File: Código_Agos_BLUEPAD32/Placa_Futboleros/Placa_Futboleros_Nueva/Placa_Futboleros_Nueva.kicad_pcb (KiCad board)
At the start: 2 copper layers, 72 x 72 mm, 18 parts, among them J1 BAT, J2 Motor_Izq_Adelante, J3 Motor_Izq_Atras, J4 Motor_Der_Adelante, J5 Motor_Der_Atras, U1 AMS1117, U2 esp32_36_pins-custom_library, U3 DRV8833, U4 DRV8833

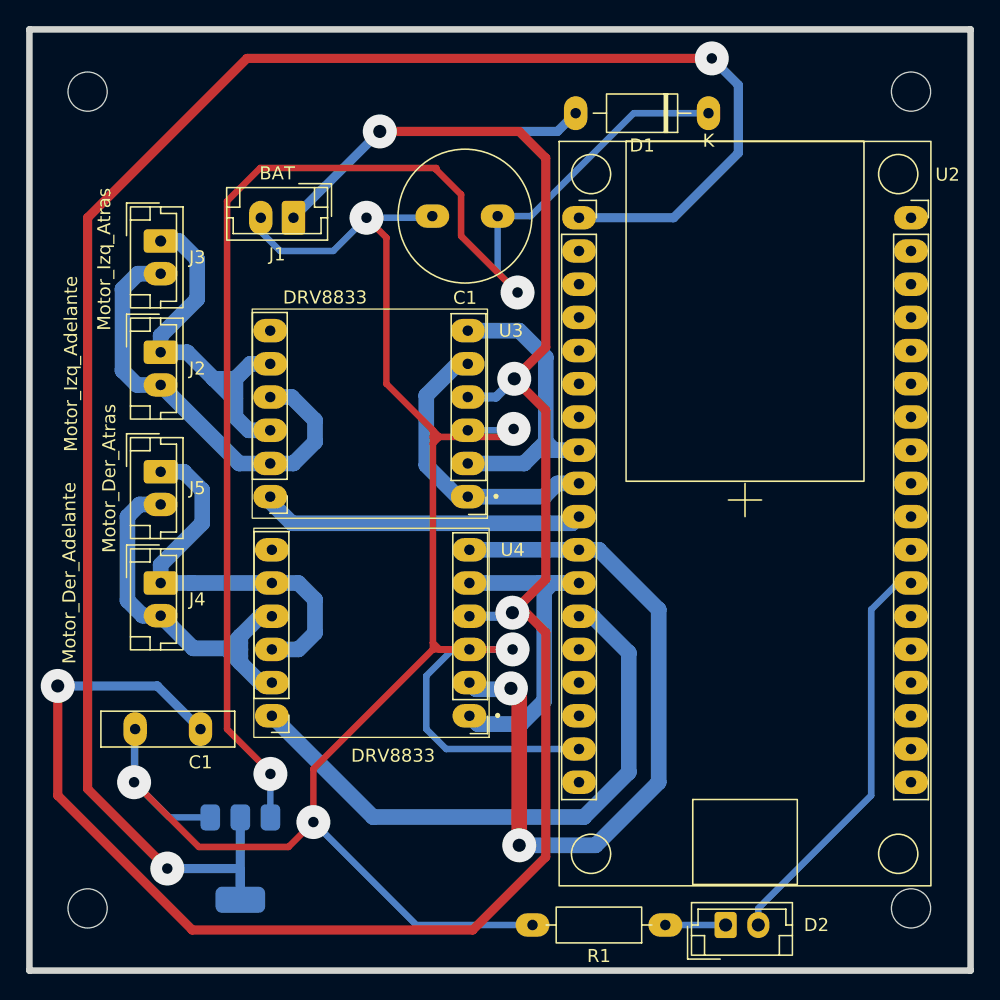
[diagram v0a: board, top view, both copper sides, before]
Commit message: Reorganización de carpetas
Se reordena algunas carpetas para mayor entendimiento...

También se adiciona el archivo original con links importantes
que contienen la información desde donde se empezó este proyecto.
> Tener en cuenta que algunos links pueden ya no estar disponibles, revisar.
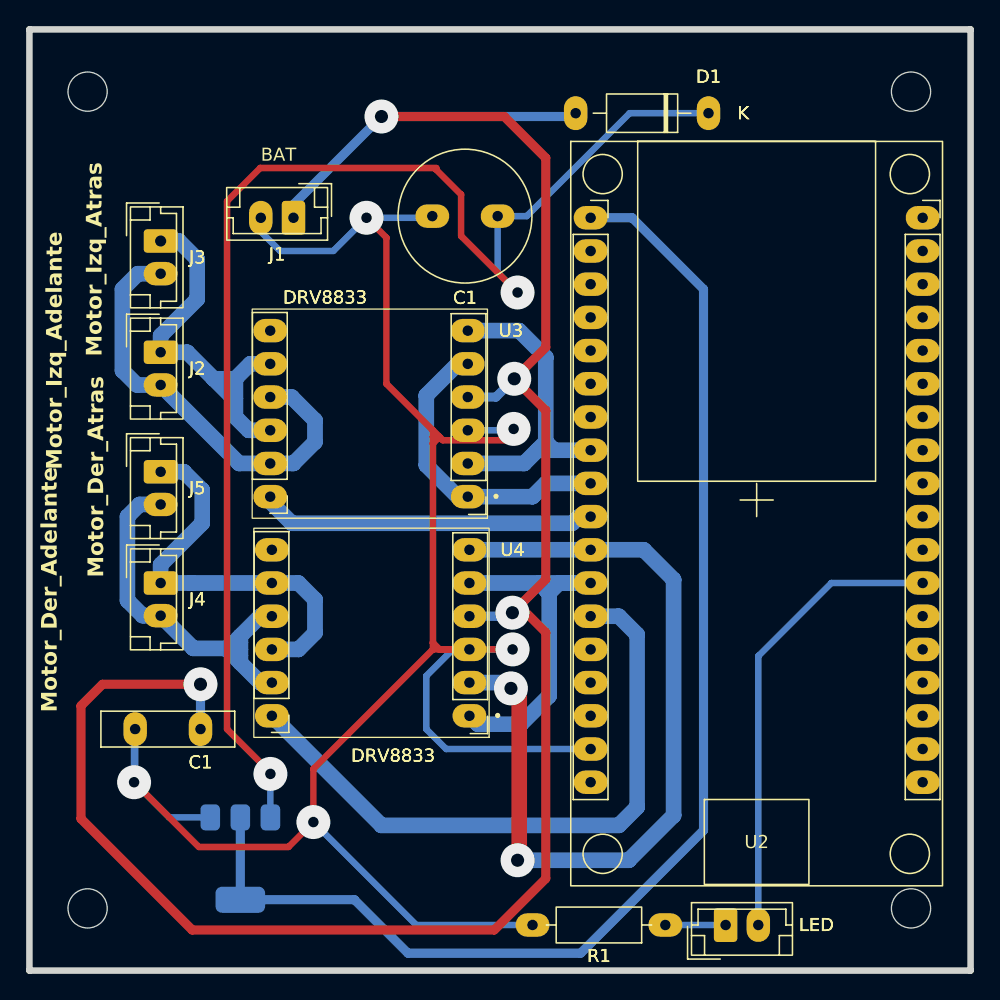
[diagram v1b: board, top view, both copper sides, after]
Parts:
- moved U2 0.89 mm to (109.1, 46.7)
- renumbered D2 to LED
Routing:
- net +5V: track 141.7 -> 99.6 mm, vias 2 -> 0
- net IN_M2B: track 57.9 -> 64.8 mm
- net LED_Encendido: track 31.6 -> 35.5 mm
- net SLEEP_M2: track 46.0 -> 49.3 mm
- net IN_M2A: track 27.1 -> 29.0 mm
- net GND: track 163.8 -> 164.9 mm
- net SLEEP_M1: track 24.9 -> 25.8 mm
- net IN_M1B: track 24.0 -> 24.9 mm
- net IN_M1A: track 22.6 -> 23.5 mm
- net VCC: track 169.1 -> 169.7 mm
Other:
- board text added: "BAT"
- board text added: "C1"
- board text added: "D1"
- board text added: "DRV8833"
- board text added: "J1"
- board text added: "J2"
- board text added: "J3"
- board text added: "J4"
- board text added: "J5"
- board text added: "K"
- board text added: "LED"
- board text added: "Motor_Der_Adelante"
- board text added: "Motor_Der_Atras"
- board text added: "Motor_Izq_Atras"
- board text added: "R1"
- board text added: "U2"
- board text added: "U3"
- board text added: "U4"
